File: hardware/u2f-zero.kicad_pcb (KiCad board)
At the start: 2 copper layers, 40.5 x 14.5 mm, 16 parts, among them SW1 SW_PUSH

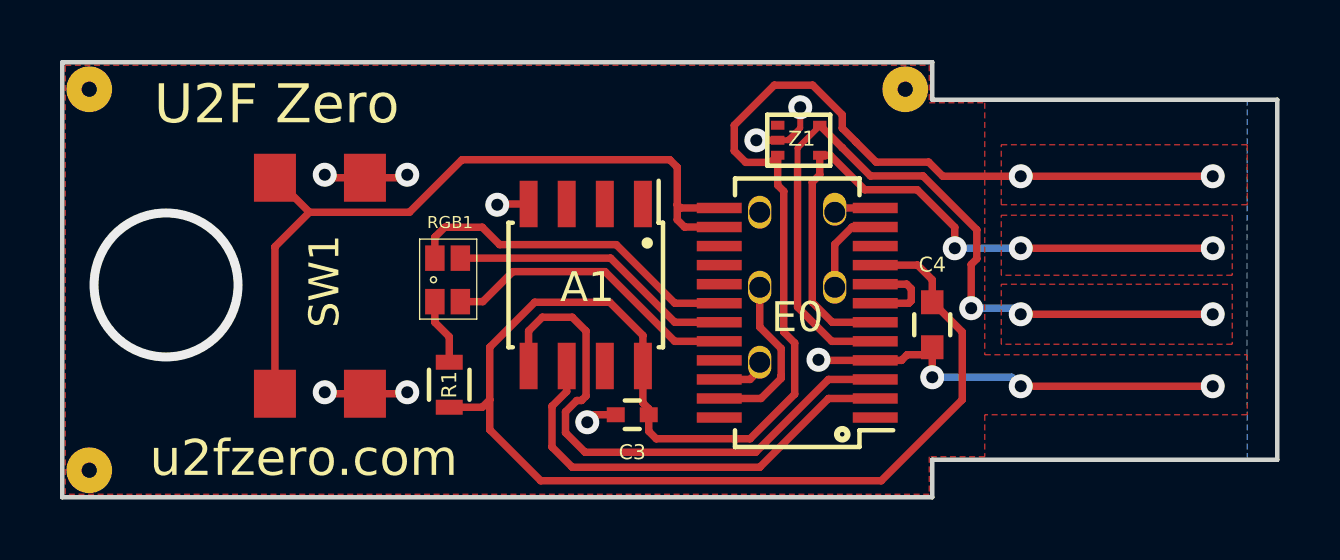
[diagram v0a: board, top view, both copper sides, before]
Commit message: Change PCB text
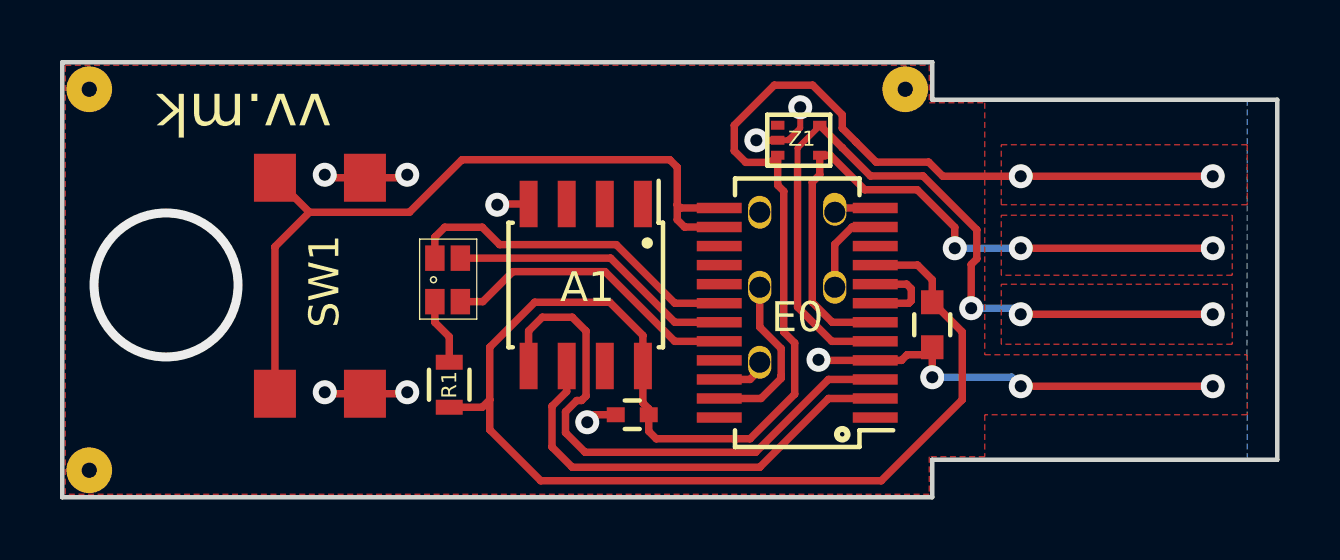
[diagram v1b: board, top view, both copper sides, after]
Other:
- board text added: "vv.mk"
- board text removed: "U2F Zero"
- board text removed: "u2fzero.com"
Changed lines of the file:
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@@
-(kicad_pcb (version 4) (host pcbnew 4.0.4+e1-6308~48~ubuntu14.04.1-stable)
+(kicad_pcb (version 4) (host pcbnew 4.0.7)
   (general
     (links 28)
     (no_connects 0)
-    (area 35.145238 27.275 76.550001 43.575001)
+    (area 33.409599 27.275 76.550001 43.575001)
     (thickness 2)
-    (drawings 50)
+    (drawings 49)
     (tracks 197)
     (zones 0)
@@
   )
   (setup
-    (last_trace_width 0.25)
+    (last_trace_width 0.2)
     (user_trace_width 0.16)
     (user_trace_width 0.2)
@@
     (visible_elements 7FFEFF3F)
     (pcbplotparams
-      (layerselection 0x010f0_80000001)
+      (layerselection 0x010fc_80000001)
       (usegerberextensions false)
-      (excludeedgelayer true)
+      (usegerberattributes true)
+      (excludeedgelayer false)
       (linewidth 0.100000)
       (plotframeref false)
@@
       (psa4output false)
       (plotreference true)
-      (plotvalue true)
+      (plotvalue false)
       (plotinvisibletext false)
       (padsonsilk false)
@@
     (tags "capacitor 0402")
     (attr smd)
-    (fp_text reference C3 (at 0 -1.25 180) (layer F.SilkS)
+    (fp_text reference C3 (at 0 -1.25 180) (layer F.SilkS) hide
       (effects (font (size 0.5 0.5) (thickness 0.125)))
     )
@@
     (tags "capacitor 0603")
     (attr smd)
-    (fp_text reference C4 (at 2 0 180) (layer F.SilkS)
+    (fp_text reference C4 (at 2 0 180) (layer F.SilkS) hide
       (effects (font (size 0.5 0.5) (thickness 0.125)))
     )
@@
     (at 48.1 36.25)
     (attr smd)
-    (fp_text reference RGB1 (at 0.07546 -1.90872) (layer F.SilkS)
+    (fp_text reference RGB1 (at 0.07546 -1.90872) (layer F.SilkS) hide
       (effects (font (size 0.4 0.4) (thickness 0.1)))
     )
@@
     (pad 1 thru_hole circle (at 0 0) (size 1.524 1.524) (drill 0.508) (layers *.Cu *.Mask F.SilkS)
       (solder_mask_margin 1.016) (clearance 1.016))
+  )
+  (gr_text vv.mk (at 41.3 30.7 180) (layer F.SilkS)
+    (effects (font (size 1.4 1.4) (thickness 0.25)))
   )
   (gr_line (start 64.09 32.44) (end 63.582 32.44) (angle 90) (layer B.SilkS) (width 0.2))
@@
   (gr_line (start 64.25 30.25) (end 64.25 29) (angle 90) (layer Edge.Cuts) (width 0.15))
   (gr_line (start 66.1 30.05) (end 66.1 42.45) (angle 90) (layer Cmts.User) (width 0.2))
-  (gr_text u2fzero.com (at 43.3 42.2) (layer F.SilkS)
-    (effects (font (size 1.2 1.2) (thickness 0.2)))
-  )
-  (gr_text "U2F Zero" (at 42.4 30.4) (layer F.SilkS)
-    (effects (font (size 1.3 1.3) (thickness 0.25)))
-  )
   (gr_line (start 75.75 42.25) (end 75.75 30.25) (angle 90) (layer Edge.Cuts) (width 0.15))
   (gr_text "GND\n" (at 64.45 40.05) (layer Cmts.User)
